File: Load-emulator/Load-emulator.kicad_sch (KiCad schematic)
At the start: 16 parts, among them J1 533980771, J2 SSW-126-04-G-D, J3 SSW-126-04-G-D, Q1 TIP41C, U1 LM318H

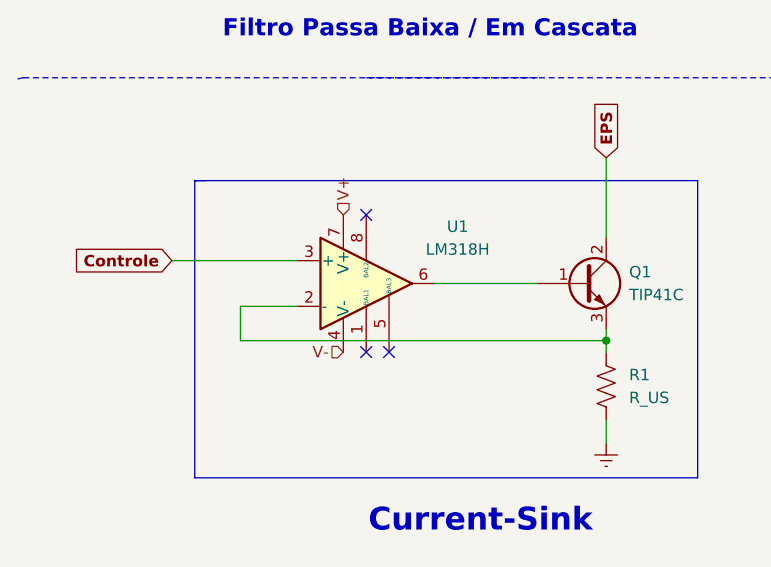
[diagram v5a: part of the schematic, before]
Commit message: minor changes in connectors
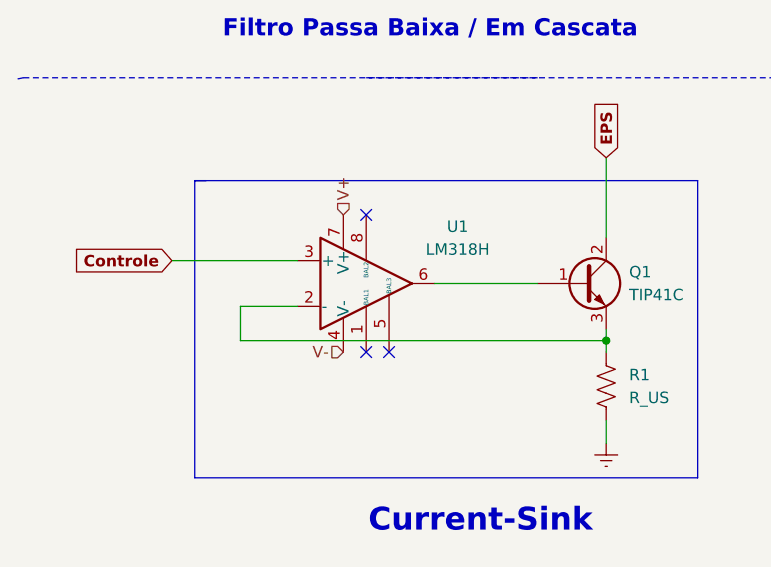
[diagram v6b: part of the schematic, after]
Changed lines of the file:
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@@
 (kicad_sch
-	(version 20231120)
+	(version 20250114)
 	(generator "eeschema")
-	(generator_version "8.0")
+	(generator_version "9.0")
 	(paper "A4")
 	(title_block
@@
 		(comment 2 "Fernanda P. Morais <Fernandapaivamorais@gmail.com>")
 	)
+	(text "PPS Bus"
+		(exclude_from_sim no)
+		(at 118.11 80.01 0)
+		(effects
+			(font
+				(size 2.5 2.5)
+			)
+			(justify left bottom)
+		)
+	)
+	(text "Enable Pin"
+		(exclude_from_sim no)
+		(at 148.59 24.13 0)
+		(effects
+			(font
+				(size 2.5 2.5)
+			)
+			(justify left bottom)
+		)
+	)
+	(text "Filtro Passa Baixa / Em Cascata\n\n"
+		(exclude_from_sim no)
+		(at 57.912 83.82 0)
+		(effects
+			(font
+				(size 1.905 1.905)
+				(thickness 0.254)
+				(bold yes)
+			)
+		)
+	)
+	(text "PC / 104 BUS"
+		(exclude_from_sim no)
+		(at 196.088 106.68 0)
+		(effects
+			(font
+				(size 3.81 3.81)
+				(thickness 0.254)
+				(bold yes)
+			)
+		)
+	)
+	(text "Conector- Picoblade 7 channels\n \n"
+		(exclude_from_sim no)
+		(at 59.944 46.228 0)
+		(effects
+			(font
+				(size 2.032 2.032)
+			)
+		)
+	)
+	(text "Current-Sink"
+		(exclude_from_sim no)
+		(at 63.5 136.906 0)
+		(effects
+			(font
+				(size 2.54 2.54)
+				(thickness 0.254)
+				(bold yes)
+			)
+		)
+	)
+	(text "GND"
+		(exclude_from_sim no)
+		(at 120.65 40.64 0)
+		(effects
+			(font
+				(size 2.5 2.5)
+			)
+			(justify left bottom)
+		)
+	)
+	(text "Voltage Input Pin"
+		(exclude_from_sim no)
+		(at 138.684 59.182 0)
+		(effects
+			(font
+				(size 2.5 2.5)
+			)
+			(justify left bottom)
+		)
+	)
+	(text "CAN Bus"
+		(exclude_from_sim no)
+		(at 116.84 24.13 0)
+		(effects
+			(font
+				(size 2.5 2.5)
+			)
+			(justify left bottom)
+		)
+	)
+	(text "UART Bus"
+		(exclude_from_sim no)
+		(at 116.84 67.31 0)
+		(effects
+			(font
+				(size 2.5 2.5)
+			)
+			(justify left bottom)
+		)
+	)
 	(junction
 		(at 124.46 43.18)
@@
 		)
 	)
-	(text "PPS Bus"
-		(exclude_from_sim no)
-		(at 118.11 80.01 0)
-		(effects
-			(font
-				(size 2.5 2.5)
-			)
-			(justify left bottom)
-		)
-	)
-	(text "Enable Pin"
-		(exclude_from_sim no)
-		(at 148.59 24.13 0)
-		(effects
-			(font
-				(size 2.5 2.5)
-			)
-			(justify left bottom)
-		)
-	)
-	(text "Filtro Passa Baixa / Em Cascata\n\n"
-		(exclude_from_sim no)
-		(at 57.912 83.82 0)
-		(effects
-			(font
-				(size 1.905 1.905)
-				(thickness 0.254)
-				(bold yes)
-			)
-		)
-	)
-	(text "PC / 104 BUS"
-		(exclude_from_sim no)
-		(at 196.088 106.68 0)
-		(effects
-			(font
-				(size 3.81 3.81)
-				(thickness 0.254)
-				(bold yes)
-			)
-		)
-	)
-	(text "Conector- Picoblade 7 channels\n \n"
-		(exclude_from_sim no)
-		(at 59.944 46.228 0)
-		(effects
-			(font
-				(size 2.032 2.032)
-			)
-		)
-	)
-	(text "Current-Sink"
-		(exclude_from_sim no)
-		(at 63.5 136.906 0)
-		(effects
-			(font
-				(size 2.54 2.54)
-				(thickness 0.254)
-				(bold yes)
-			)
-		)
-	)
-	(text "GND"
-		(exclude_from_sim no)
-		(at 120.65 40.64 0)
-		(effects
-			(font
-				(size 2.5 2.5)
-			)
-			(justify left bottom)
-		)
-	)
-	(text "Voltage Input Pin"
-		(exclude_from_sim no)
-		(at 138.684 59.182 0)
-		(effects
-			(font
-				(size 2.5 2.5)
-			)
-			(justify left bottom)
-		)
-	)
-	(text "CAN Bus"
-		(exclude_from_sim no)
-		(at 116.84 24.13 0)
-		(effects
-			(font
-				(size 2.5 2.5)
-			)
-			(justify left bottom)
-		)
-	)
-	(text "UART Bus"
-		(exclude_from_sim no)
-		(at 116.84 67.31 0)
-		(effects
-			(font
-				(size 2.5 2.5)
-			)
-			(justify left bottom)
-		)
-	)
 	(label "DGND"
 		(at 215.9 63.5 0)
-		(fields_autoplaced yes)
 		(effects
 			(font
@@
 	(label "H2-08"
 		(at 165.1 46.99 0)
-		(fields_autoplaced yes)
 		(effects
 			(font
@@
 	(label "EN_SWITCH"
 		(at 149.86 39.37 180)
-		(fields_autoplaced yes)
 		(effects
 			(font
@@
 	(label "LR_GPS_IN"
 		(at 125.73 82.55 0)
-		(fields_autoplaced yes)
 		(effects
 			(font
@@
 	(label "DGND"
 		(at 231.14 63.5 180)
-		(fields_autoplaced yes)
 		(effects
 			(font
@@
 	(label "DGND"
 		(at 266.7 60.96 0)
-		(fields_autoplaced yes)
 		(effects
 			(font
@@
 	(label "H1-49"
 		(at 160.02 73.66 0)
-		(fields_autoplaced yes)
 		(effects
 			(font
@@
 	(label "H1-01"
 		(at 123.19 26.67 180)
-		(fields_autoplaced yes)
 		(effects
 			(font
@@
 	(label "CAN_N"
 		(at 125.73 26.67 0)
-		(fields_autoplaced yes)
 		(effects
 			(font
@@
 	(label "H1-47"
 		(at 160.02 66.04 0)
-		(fields_autoplaced yes)
 		(effects
 			(font
@@
 	(label "H1-02"
 		(at 123.19 82.55 180)
-		(fields_autoplaced yes)
 		(effects
 			(font
@@
 	(label "H1-32"
 		(at 121.92 50.8 180)
-		(fields_autoplaced yes)
 		(effects
 			(font
@@
 	(label "5V"
 		(at 144.78 73.66 180)
-		(fields_autoplaced yes)
 		(effects
 			(font
@@
 	(label "H2-30"
 		(at 127 48.26 0)
-		(fields_autoplaced yes)
 		(effects
 			(font
@@
 	(label "H1-19"
 		(at 123.19 72.39 180)
-		(fields_autoplaced yes)
 		(effects
 			(font
@@
 	(label "H1-17"
 		(at 123.19 69.85 180)
-		(fields_autoplaced yes)
 		(effects
 			(font
@@
 	(label "DGND"
 		(at 266.7 63.5 0)
-		(fields_autoplaced yes)
 		(effects
 			(font
@@
 	(label "H2-04"
 		(at 165.1 39.37 0)
-		(fields_autoplaced yes)
 		(effects
 			(font
@@
 	(label "H1-29"
 		(at 121.92 43.18 180)
-		(fields_autoplaced yes)
 		(effects
 			(font
@@
 	(label "DGND"
 		(at 215.9 60.96 0)
-		(fields_autoplaced yes)
 		(effects
 			(font
@@
 	(label "DGND"
 		(at 180.34 63.5 180)
-		(fields_autoplaced yes)
 		(effects
 			(font
@@
 	(label "H1-31"
 		(at 121.92 45.72 180)
-		(fields_autoplaced yes)
 		(effects
 			(font
@@
 	(label "H2-32"
 		(at 127 50.8 0)
-		(fields_autoplaced yes)
 		(effects
 			(font
@@
 	(label "H2-31"
 		(at 127 45.72 0)
-		(fields_autoplaced yes)
 		(effects
 			(font
@@
 	(label "DGND"
 		(at 180.34 60.96 180)
-		(fields_autoplaced yes)
 		(effects
 			(font
@@
 	(label "H1-03"
 		(at 123.19 29.21 180)
-		(fields_autoplaced yes)
 		(effects
 			(font
@@
 	(label "H1-30"
 		(at 121.92 48.26 180)
-		(fields_autoplaced yes)
 		(effects
 			(font
@@
 	(label "H2-29"
 		(at 127 43.18 0)
-		(fields_autoplaced yes)
 		(effects
 			(font
@@
 	(label "H2-03"
 		(at 165.1 31.75 0)
-		(fields_autoplaced yes)
 		(effects
 			(font
@@
 	(label "CAN_P"
 		(at 125.73 29.21 0)
-		(fields_autoplaced yes)
 		(effects
 			(font
@@
 	(label "UART_RX"
 		(at 125.73 72.39 0)
-		(fields_autoplaced yes)
 		(effects
 			(font
@@
 	(label "DGND"
 		(at 231.14 60.96 180)
-		(fields_autoplaced yes)
 		(effects
 			(font
@@
 	(label "UART_TX"
 		(at 125.73 69.85 0)
-		(fields_autoplaced yes)
 		(effects
 			(font
@@
 	(label "H1-51"
 		(at 160.02 81.28 0)
-		(fields_autoplaced yes)
 		(effects
 			(font
@@
 		(shape input)
 		(at 48.26 102.87 90)
-		(fields_autoplaced yes)
 		(effects
 			(font
@@
 		(shape input)
 		(at 48.26 118.11 180)
-		(fields_autoplaced yes)
 		(effects
 			(font
@@
 		(at 139.7 127)
 		(size 35.56 20.32)
+		(exclude_from_sim no)
+		(in_bom yes)
+		(on_board yes)
+		(dnp no)
 		(fields_autoplaced yes)
 		(stroke
@@
 		)
 	)
+	(embedded_fonts no)
 )
